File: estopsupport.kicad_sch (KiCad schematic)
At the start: 27 parts, among them J1 Barrier Block 1x3, J2 Dupont 1x2, J3 Dupont 1x2, J4 Dupont 1x2, J5 Dupont 2x4, K1 QLRELAY JQX-V7H 012-1HP, Q1 2N7002, U1 BTS6163D, U2 PC817

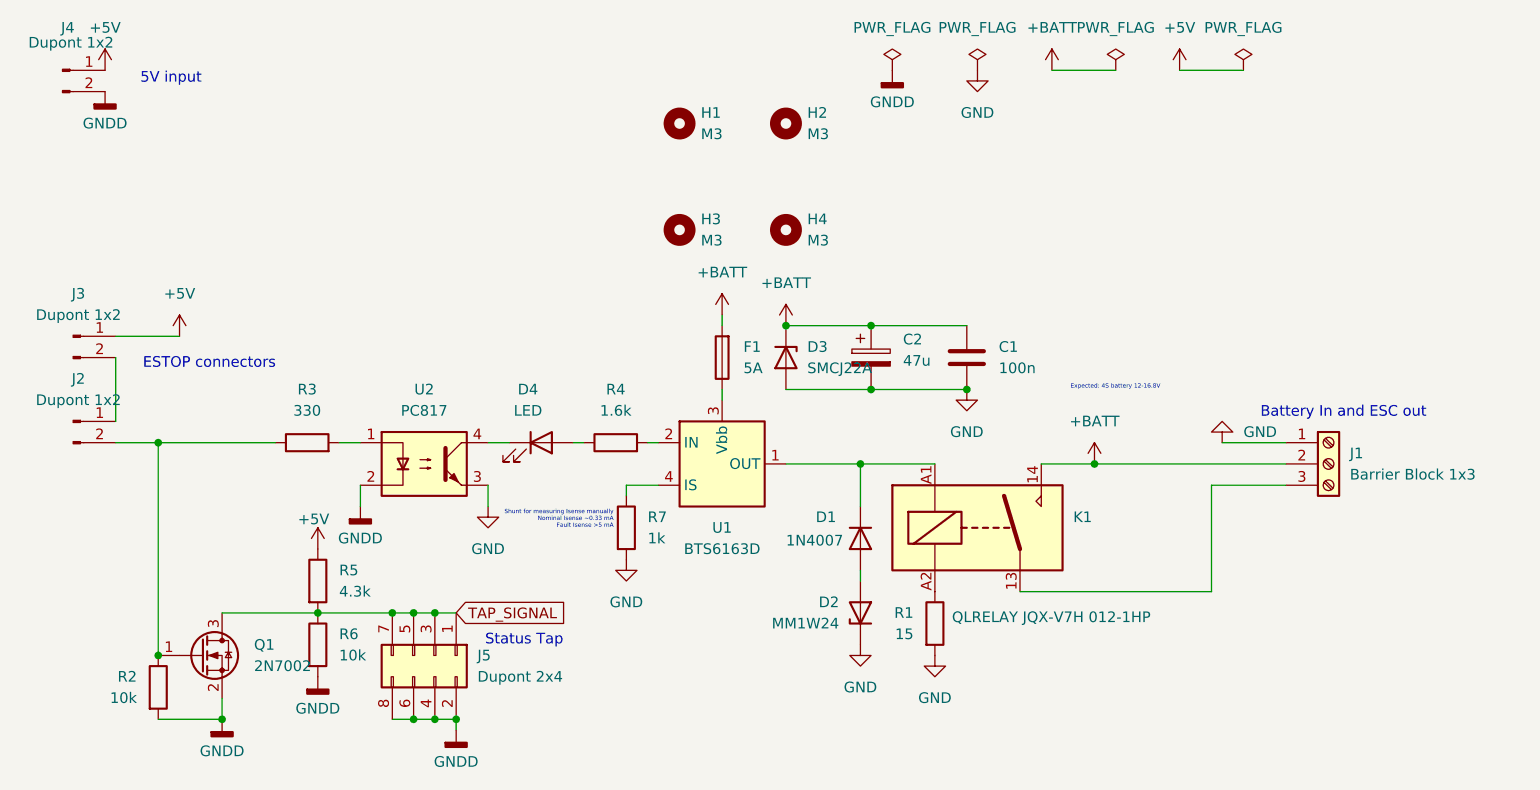
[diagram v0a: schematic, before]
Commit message: feat: change to 4 layers, put everything on the top layer so that it can be assembled by jlcpcb cheaply
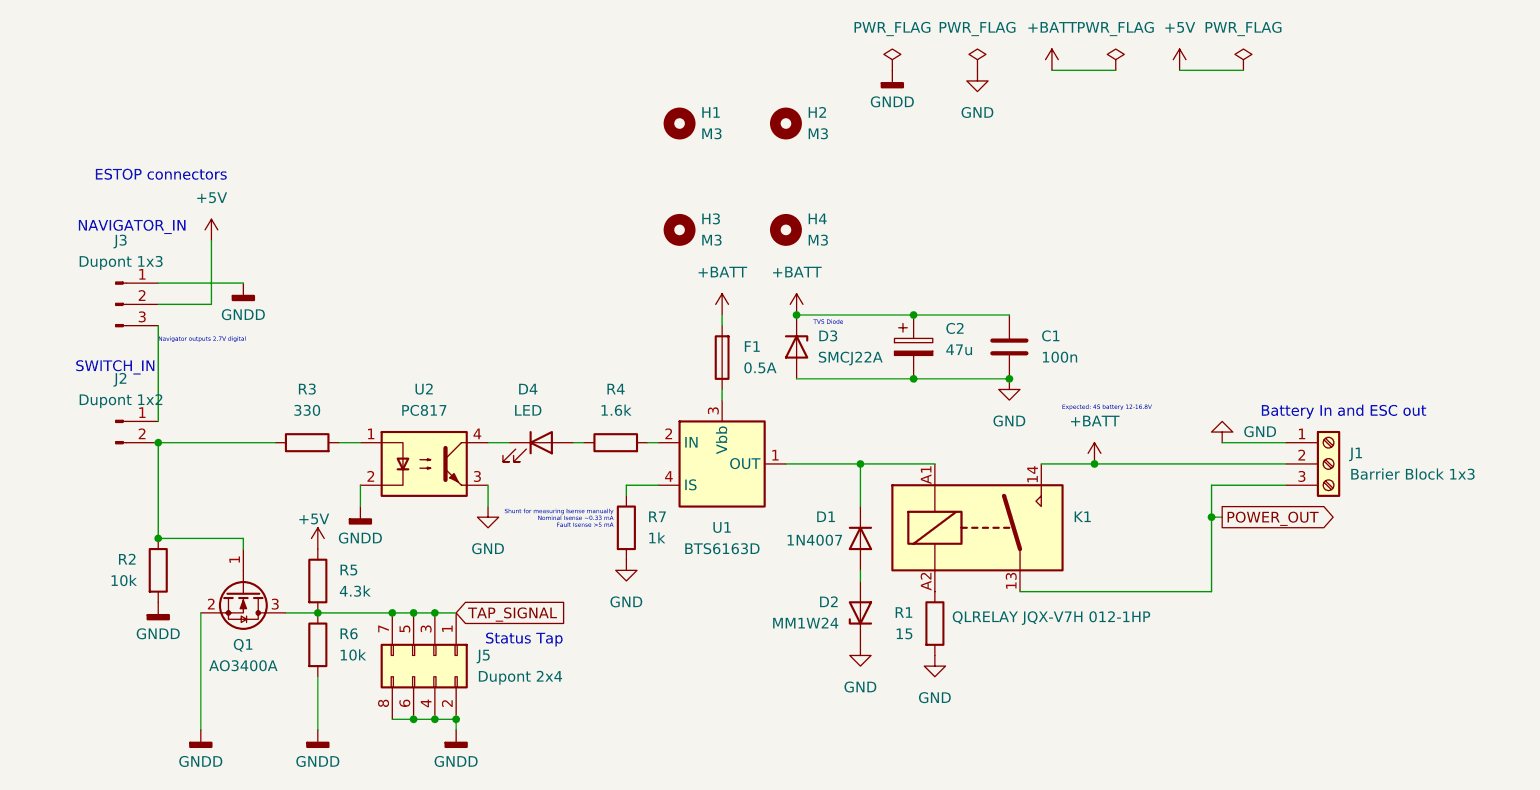
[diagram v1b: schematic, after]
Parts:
- removed J4: Dupont 1x2, Connector_PinHeader_2.54mm:PinHeader_1x02_P2.54mm_Horizontal, symbol Connector:Conn_01x02_Pin
- F1: value 5A -> 0.5A
- J3: value Dupont 1x2 -> Dupont 1x3; footprint Connector_PinHeader_2.54mm:PinHeader_1x02_P2.54mm_Horizontal -> Connector_PinHeader_2.54mm:PinHeader_1x03_P2.54mm_Horizontal; symbol Connector:Conn_01x02_Pin -> Connector:Conn_01x03_Pin
- Q1: value 2N7002 -> AO3400A
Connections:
- net +5V: now also J3.2 (Pin_2); no longer J3.1 (Pin_1)
- net GNDD: now also J3.1 (Pin_1)
- net POWER_OUT: now reaches J1.3 (Pin_3), K1.13
- net at J2.1 (Pin_1): now also J3.3 (Pin_3); no longer J3.2 (Pin_2)
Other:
- note added: "NAVIGATOR_IN"
- note added: "Navigator outputs 2.7V digital"
- note added: "SWITCH_IN"
- note added: "TVS Diode"
- note removed: "5V input"
- moved on the sheet: C1, C2, D3, J2, Q1, R2

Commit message: reverse fuse protection, silkscreen adjust and check for production
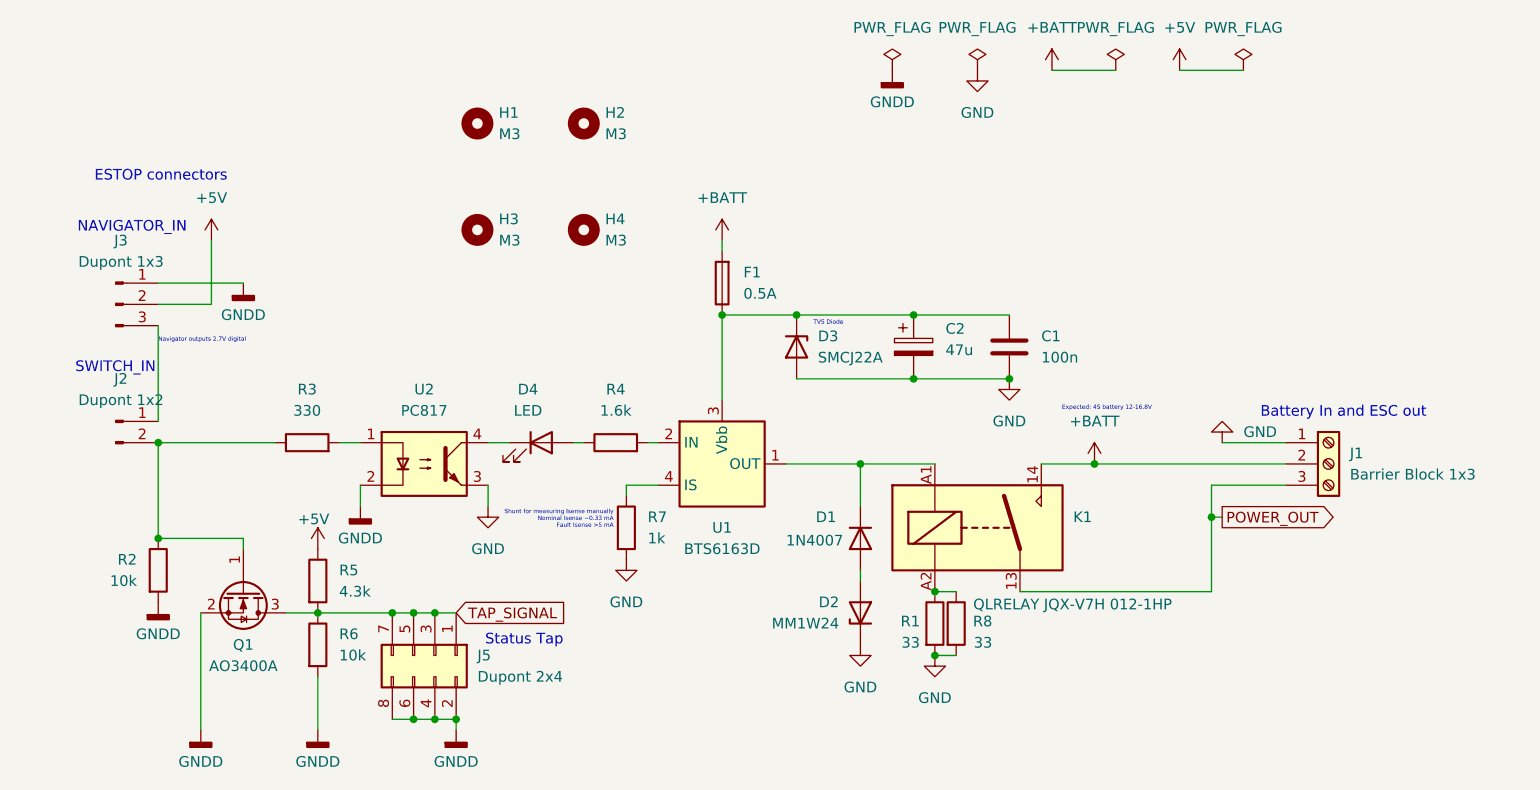
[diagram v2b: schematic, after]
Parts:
- added R8: 33, Resistor_SMD:R_1812_4532Metric, symbol Device:R
- R1: value 15 -> 33
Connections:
- net +BATT: no longer C1.1, C2.1, D3.1 (K)
- net GND: now also R8.2
- net at K1.A2, R1.1: now also R8.1
- net at F1.1, U1.3 (Vbb): now also C1.1, C2.1, D3.1 (K)
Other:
- moved on the sheet: F1, H1, H2, H3, H4
